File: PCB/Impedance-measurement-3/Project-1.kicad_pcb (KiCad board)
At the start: 2 copper layers, 112 x 88 mm, 74 parts, among them J2 USB_C_Receptacle, U1 STM32F303CCT6, U2 W25Q32JVSSIQ, U5 LM7805_TO220, U9 OPA4141AID

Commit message: schematic and layout changed 26/7/2026
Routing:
- net VDD: track 316.0 -> 309.3 mm
- net GND: track 652.4 -> 653.7 mm
- net /M-PB13: track 101.8 -> 101.3 mm
- net Net-(SWD-connector1-SWDCLK): track 275.5 -> 275.0 mm
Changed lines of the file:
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@@
 		(tags "Integrated Circuit")
 		(property "Reference" "Voltage-reference1"
-			(at -1.1 -3.05 0)
+			(at -1.1 -3.87 0)
 			(layer "F.SilkS")
 			(effects
@@
 		(tags "capacitor")
 		(property "Reference" "C18-100nF1"
-			(at 0 -1.68 0)
+			(at 0 -3 0)
 			(layer "F.SilkS")
 			(effects
@@
 		(descr "2x10 0.05in shrouded male header")
 		(property "Reference" "SWD-connector1"
-			(at 9.080665 0.265167 0)
+			(at 0.46 -3.365 0)
 			(layer "F.SilkS")
 			(effects
@@
 		)
 		(property "Value" "SWD"
-			(at -1.54 4.545 0)
+			(at 1.46 3.365 0)
 			(layer "F.Fab")
 			(effects
@@
 		(pad "1" thru_hole circle
 			(at -2.54 0.635)
-			(size 0.8128 0.8128)
+			(size 0.96 0.96)
 			(drill 0.75)
 			(layers "*.Cu" "*.Mask")
@@
 		(pad "2" thru_hole circle
 			(at -2.54 -0.635)
-			(size 0.8128 0.8128)
+			(size 0.96 0.96)
 			(drill 0.75)
 			(layers "*.Cu" "*.Mask")
@@
 		(pad "3" thru_hole circle
 			(at -1.27 0.635)
-			(size 0.8128 0.8128)
+			(size 0.96 0.96)
 			(drill 0.75)
 			(layers "*.Cu" "*.Mask")
@@
 		(pad "4" thru_hole circle
 			(at -1.27 -0.635)
-			(size 0.8128 0.8128)
+			(size 0.96 0.96)
 			(drill 0.75)
 			(layers "*.Cu" "*.Mask")
@@
 		(pad "5" thru_hole circle
 			(at 0 0.635)
-			(size 0.8128 0.8128)
+			(size 0.96 0.96)
 			(drill 0.75)
 			(layers "*.Cu" "*.Mask")
@@
 		(pad "6" thru_hole circle
 			(at 0 -0.625)
-			(size 0.8128 0.8128)
+			(size 0.96 0.96)
 			(drill 0.75)
 			(layers "*.Cu" "*.Mask")
@@
 		(pad "7" thru_hole circle
 			(at 1.27 0.635)
-			(size 0.8128 0.8128)
+			(size 0.96 0.96)
 			(drill 0.75)
 			(layers "*.Cu" "*.Mask")
@@
 		(pad "8" thru_hole circle
 			(at 1.27 -0.635)
-			(size 0.8128 0.8128)
+			(size 0.96 0.96)
 			(drill 0.75)
 			(layers "*.Cu" "*.Mask")
@@
 		(pad "9" thru_hole circle
 			(at 2.54 0.635)
-			(size 0.8128 0.8128)
+			(size 0.96 0.96)
 			(drill 0.75)
 			(layers "*.Cu" "*.Mask")
@@
 		(pad "10" thru_hole circle
 			(at 2.54 -0.635)
-			(size 0.8128 0.8128)
+			(size 0.96 0.96)
 			(drill 0.75)
 			(layers "*.Cu" "*.Mask")
@@
 	)
 	(segment
+		(start 117.480761 88.6)
+		(end 117.730761 88.35)
+		(width 0.1)
+		(layer "F.Cu")
+		(net 4)
+	)
+	(segment
 		(start 137.43 85.57)
 		(end 136 85.57)
@@
 	)
 	(segment
+		(start 118.08 88.005)
+		(end 118.08 87.09)
+		(width 0.1)
+		(layer "F.Cu")
+		(net 4)
+	)
+	(segment
 		(start 78.5 80.55)
 		(end 82.95 85)
@@
 	)
 	(segment
+		(start 115.54 87.54)
+		(end 116.6 88.6)
+		(width 0.1)
+		(layer "F.Cu")
+		(net 4)
+	)
+	(segment
 		(start 134 66)
 		(end 134 67)
@@
 	)
 	(segment
-		(start 115.54 87.09)
-		(end 116.37 87.92)
-		(width 0.1)
-		(layer "F.Cu")
-		(net 4)
-	)
-	(segment
 		(start 145.08 93.87)
 		(end 146.95 92)
@@
 	)
 	(segment
-		(start 117.25 87.92)
-		(end 118.08 87.09)
-		(width 0.1)
-		(layer "F.Cu")
-		(net 4)
-	)
-	(segment
 		(start 148.17 45.83)
 		(end 148.17 44.32)
@@
 	)
 	(segment
+		(start 116.6 88.6)
+		(end 117.480761 88.6)
+		(width 0.1)
+		(layer "F.Cu")
+		(net 4)
+	)
+	(segment
+		(start 115.54 87.09)
+		(end 115.54 87.54)
+		(width 0.1)
+		(layer "F.Cu")
+		(net 4)
+	)
+	(segment
 		(start 106 70)
 		(end 107 71)
@@
 	)
 	(segment
-		(start 116 92)
-		(end 116 92.07)
-		(width 0.1)
-		(layer "F.Cu")
-		(net 4)
-	)
-	(segment
 		(start 94 58)
 		(end 94 59)
@@
 	)
 	(segment
+		(start 117.735 88.35)
+		(end 118.08 88.005)
+		(width 0.1)
+		(layer "F.Cu")
+		(net 4)
+	)
+	(segment
 		(start 65.85 44.392183)
 		(end 65.85 45.17)
@@
 	)
 	(segment
+		(start 117.730761 88.35)
+		(end 117.735 88.35)
+		(width 0.1)
+		(layer "F.Cu")
+		(net 4)
+	)
+	(segment
 		(start 96 77)
 		(end 98 79)
@@
 	)
 	(segment
-		(start 116.37 87.92)
-		(end 117.25 87.92)
-		(width 0.1)
-		(layer "F.Cu")
-		(net 4)
-	)
-	(segment
 		(start 159.75 84.82)
 		(end 159.75 88.82)
@@
 	)
 	(segment
-		(start 114 53.57)
-		(end 120.75 53.57)
-		(width 0.1)
-		(layer "B.Cu")
-		(net 9)
-	)
-	(segment
 		(start 123 81)
 		(end 121 83)
@@
 	)
 	(segment
-		(start 122 93)
-		(end 120 93)
-		(width 0.1)
-		(layer "B.Cu")
-		(net 23)
-	)
-	(segment
 		(start 117 90)
 		(end 112 90)
@@
 	)
 	(segment
-		(start 124 91)
-		(end 122 93)
-		(width 0.1)
-		(layer "B.Cu")
-		(net 23)
-	)
-	(segment
-		(start 124 90)
-		(end 124 91)
-		(width 0.1)
-		(layer "B.Cu")
-		(net 23)
-	)
-	(segment
-		(start 92 95)
-		(end 92 90)
+		(start 133 90)
+		(end 124 90)
 		(width 0.1)
 		(layer "B.Cu")
@@
 	)
 	(segment
-		(start 93 96)
-		(end 92 95)
+		(start 120 93)
+		(end 117 90)
 		(width 0.1)
 		(layer "B.Cu")
@@
 	)
 	(segment
-		(start 112 90)
-		(end 106 96)
+		(start 124 90)
+		(end 121 93)
 		(width 0.1)
 		(layer "B.Cu")
@@
 	)
 	(segment
-		(start 120 93)
-		(end 117 90)
+		(start 93 96)
+		(end 92 95)
 		(width 0.1)
 		(layer "B.Cu")
@@
 	)
 	(segment
-		(start 133 90)
-		(end 124 90)
+		(start 106 96)
+		(end 93 96)
 		(width 0.1)
 		(layer "B.Cu")
@@
 	)
 	(segment
-		(start 106 96)
-		(end 93 96)
+		(start 112 90)
+		(end 106 96)
+		(width 0.1)
+		(layer "B.Cu")
+		(net 23)
+	)
+	(segment
+		(start 92 95)
+		(end 92 90)
 		(width 0.1)
 		(layer "B.Cu")
@@
 	)
 	(segment
+		(start 121 93)
+		(end 120 93)
+		(width 0.1)
+		(layer "B.Cu")
+		(net 23)
+	)
+	(segment
 		(start 111.282843 79.636396)
 		(end 111.282843 80.202082)
@@
 	)
 	(segment
+		(start 118 89)
+		(end 116 89)
+		(width 0.1)
+		(layer "F.Cu")
+		(net 31)
+	)
+	(segment
 		(start 156.275075 67.27)
 		(end 157.144925 67.27)
@@
 	)
 	(segment
-		(start 118 89)
-		(end 116.884314 89)
-		(width 0.1)
-		(layer "F.Cu")
-		(net 31)
-	)
-	(segment
 		(start 149 60)
 		(end 152 60)
@@
 	)
 	(segment
-		(start 116.884314 89)
-		(end 115.884314 88)
+		(start 148.282843 60.717157)
+		(end 149.4 61.834314)
 		(width 0.1)
 		(layer "F.Cu")
@@
 	)
 	(segment
-		(start 148.282843 60.717157)
-		(end 149.4 61.834314)
+		(start 116 89)
+		(end 115 88)
 		(width 0.1)
 		(layer "F.Cu")
@@
 	)
 	(segment
-		(start 115.884314 88)
-		(end 109 88)
-		(width 0.1)
-		(layer "F.Cu")
-		(net 31)
-	)
-	(segment
 		(start 142 76)
 		(end 141 77)
@@
 	)
 	(segment
-		(start 110.45 83.55)
-		(end 111 83.55)
+		(start 156.225685 69.37)
+		(end 149.595685 76)
 		(width 0.1)
 		(layer "F.Cu")
@@
 	)
 	(segment
-		(start 156.225685 69.37)
-		(end 149.595685 76)
+		(start 149.595685 76)
+		(end 142 76)
 		(width 0.1)
 		(layer "F.Cu")
@@
 	)
 	(segment
-		(start 149.595685 76)
-		(end 142 76)
+		(start 115 88)
+		(end 109 88)
 		(width 0.1)
 		(layer "F.Cu")

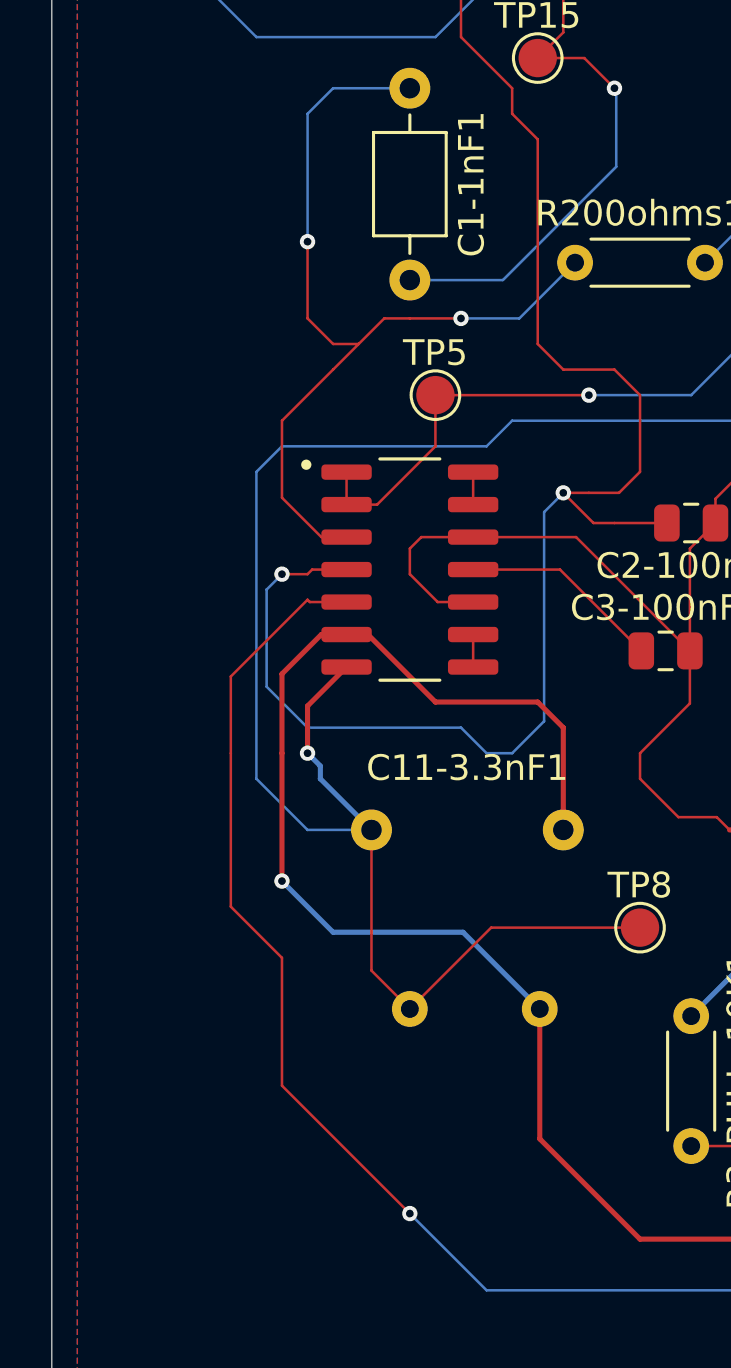
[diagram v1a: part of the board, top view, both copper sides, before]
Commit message: schematic and layout changed second time in 26/7/2026
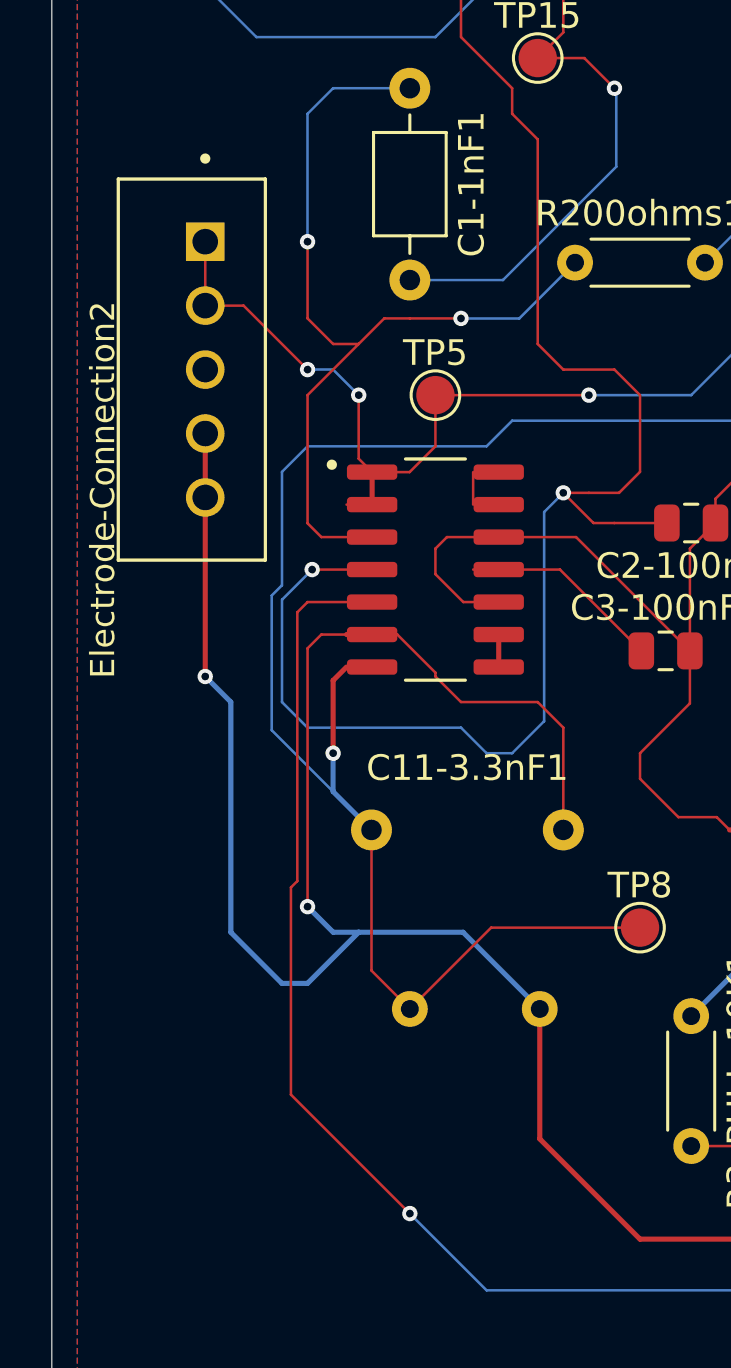
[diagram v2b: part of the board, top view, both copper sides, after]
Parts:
- added Electrode-Connection2: Cable-connector B5B-XH-A_LF__SN_, Connector:JST_B5B-XH-A_LF__SN_, F.Cu at (63.5, 74.0)
- moved U9 1.00 mm to (73.0, 81.8)
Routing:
- net /Electrode2: track 85.9 -> 111.5 mm, vias 1 -> 2
- net /Electrode1: track 106.4 -> 119.3 mm, vias 6 -> 8
- net Net-(U1-PA1): track 158.1 -> 154.7 mm
- net Net-(U9-+IN_B): track 128.7 -> 126.6 mm
- net GND: track 653.7 -> 651.7 mm
- net /VBUS-5V: track 347.9 -> 346.8 mm
- net Net-(U9-+IN_A): track 35.0 -> 34.2 mm
